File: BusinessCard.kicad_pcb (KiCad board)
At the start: 4 copper layers, 88.9 x 50.8 mm, 81 parts, among them J1 USB_OTG, J5 RNG, Q1 2N3904, Q2 2N3904, U1 TLE2426, U10 74HC74, U11 74HC74, U12 74HC74, U13 74HC74, U2 TLV271, U3 LM311, U4 74HC74, U5 INA826, U6 TLV272, U7 4066, U8 TLV272, U9 74HC14

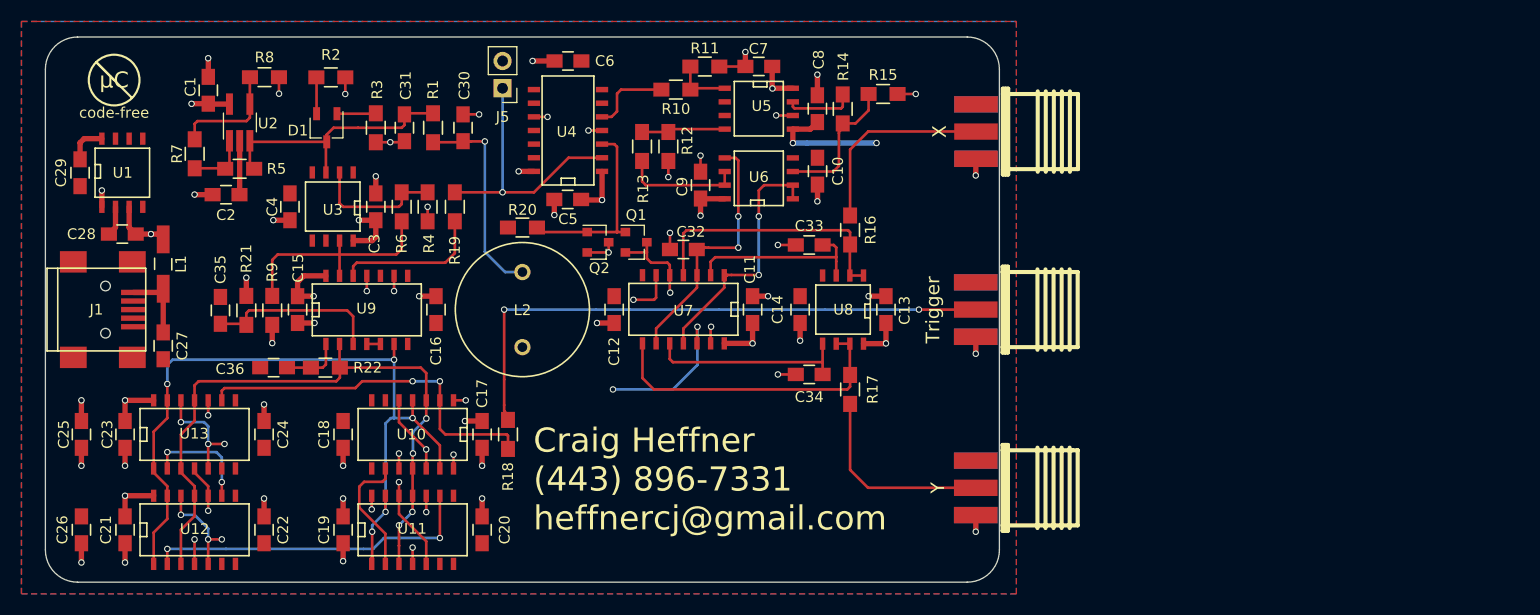
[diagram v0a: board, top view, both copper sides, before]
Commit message: All but the ring counter placed and routed.
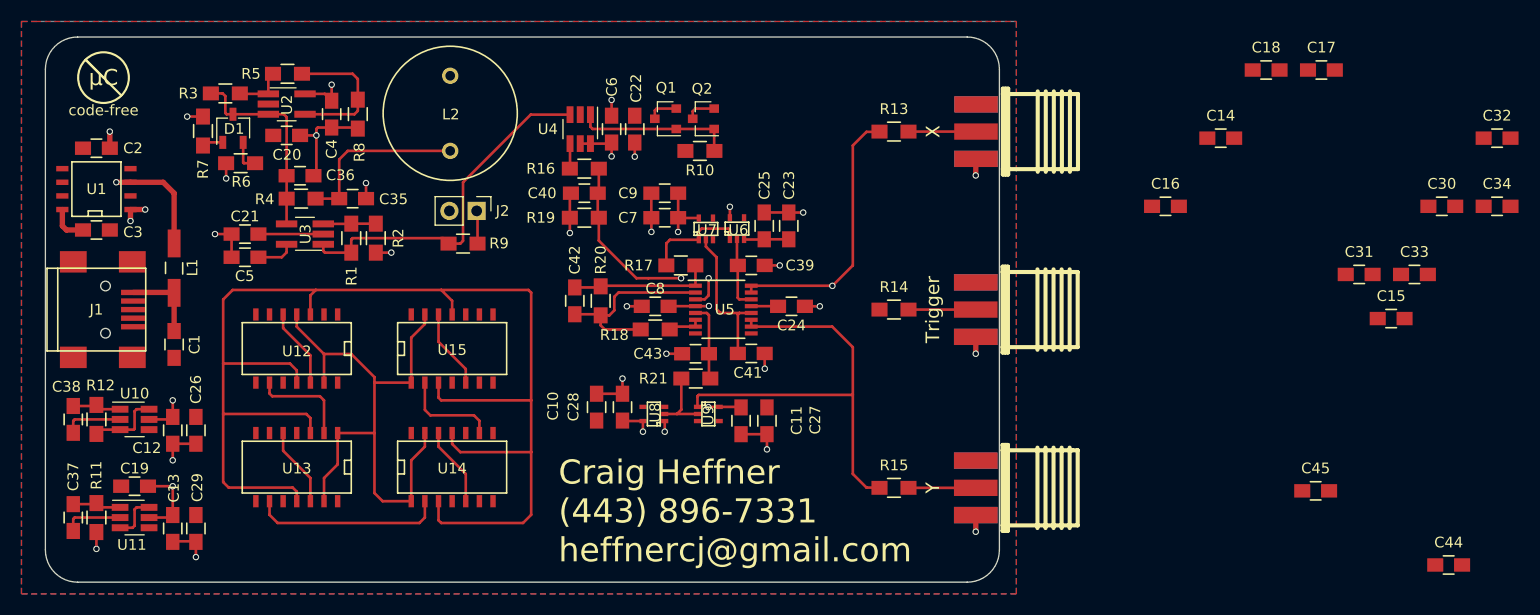
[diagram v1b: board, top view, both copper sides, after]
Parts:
- removed R22: 56k, Resistors_SMD:R_0805_HandSoldering
- removed Trigger: Trigger, CON-SMA-EDGE:CON-SMA-EDGE
- removed X: X, CON-SMA-EDGE:CON-SMA-EDGE
- removed Y: Y, CON-SMA-EDGE:CON-SMA-EDGE
- added C37: 0.1uF, Capacitors_SMD:C_0805_HandSoldering, F.Cu at (107.7, 116.1)
- added C38: 0.1uF, Capacitors_SMD:C_0805_HandSoldering, F.Cu at (107.7, 106.9)
- added C39: 1500pF, Capacitors_SMD:C_0805_HandSoldering, F.Cu at (170.9, 92.6)
- added C40: 1500pF, Capacitors_SMD:C_0805_HandSoldering, F.Cu at (155.3, 85.9)
- added C41: 1500pF, Capacitors_SMD:C_0805_HandSoldering, F.Cu at (170.9, 100.8)
- added C42: 1500pF, Capacitors_SMD:C_0805_HandSoldering, F.Cu at (154.4, 95.9)
- added C43: 1500pF, Capacitors_SMD:C_0805_HandSoldering, F.Cu at (165.7, 100.8)
- added C44: 10uF, Capacitors_SMD:C_0805_HandSoldering, F.Cu at (235.9, 120.5)
- added C45: 10uF, Capacitors_SMD:C_0805_HandSoldering, F.Cu at (223.5, 113.6)
- added J2: RNG, Pin_Headers:Pin_Header_Straight_1x02_Pitch2.54mm, F.Cu at (145.3, 87.5)
- added J3: X, CON-SMA-EDGE:CON-SMA-EDGE, F.Cu at (191.8, 80.1)
- added J4: Trigger, CON-SMA-EDGE:CON-SMA-EDGE, F.Cu at (191.8, 96.7)
- added U14: 74HC74, SMD_Packages:SOIC-14_N, F.Cu at (143.0, 111.3)
- added U15: 74HC74, SMD_Packages:SOIC-14_N, F.Cu at (143.0, 100.2)
- C18, C19, C2: value 0.1uF -> 10uF
- C25, C26, C28: value 10uF -> 0.1uF
- C31: value 0.01uF -> 0.1uF
- C32, C33: value 1500pF -> 0.1uF
- C34: value 1500pF -> 10uF
- C36: value 0.1uF -> 0.01uF
- J5: value RNG -> Y; footprint Pin_Headers:Pin_Header_Straight_1x02_Pitch2.54mm -> CON-SMA-EDGE:CON-SMA-EDGE
- R1: value 1.37k -> 1M
- R10: value 15k -> 2.2k
- R11: value 10k -> 10M
- R12: value 10k -> 56k
- R13, R14, R15: value 10k -> 2.2k
- R16, R18: value 2.2k -> 1.5k
- R17: value 2.2k -> 100
- R19, R20, R3: value 2.2k -> 1k
- R2: value 2.2k -> 100k
- R21: value 10M -> 100
- R4: value 100k -> 1.37k
- R6: value 1M -> 2.2k
- R7, R9: value 1k -> 2.2k
- U10, U11: value 74HC74 -> SN74LVC2G14DBVR; footprint SMD_Packages:SOIC-14_N -> TO_SOT_Packages_SMD:SOT-23-6_Handsoldering
- U3: value LM311 -> TLV3201; footprint SMD_Packages:SOIC-8-N -> TO_SOT_Packages_SMD:TSOT-23-5_HandSoldering
- U4: value 74HC74 -> SN74LVC1G175; footprint SMD_Packages:SOIC-14_N -> TO_SOT_Packages_SMD:SOT-23-6_Handsoldering
- U5: value INA826 -> LTC6242; footprint SMD_Packages:SOIC-8-N -> Housings_SSOP:SSOP-16_3.9x4.9mm_Pitch0.635mm
- U6, U8: value TLV272 -> SN74LVC1G66; footprint SMD_Packages:SOIC-8-N -> TO_SOT_Packages_SMD:SC-70-5
- U7: value 4066 -> SN74LVC1G66; footprint SMD_Packages:SOIC-14_N -> TO_SOT_Packages_SMD:SC-70-5
- U9: value 74HC14 -> SN74LVC1G66; footprint SMD_Packages:SOIC-14_N -> TO_SOT_Packages_SMD:SC-70-5
- moved C15 101.9 mm to (230.5, 97.5), turned to 0 degrees
- moved C18 92.5 mm to (218.9, 74.4), turned to 0 degrees
- moved C30 91.5 mm to (235.2, 87.1), turned to 0 degrees
- moved C31 90.0 mm to (227.5, 93.4), turned to 0 degrees
- moved C17 85.3 mm to (224.0, 74.4), turned to 0 degrees
- moved C32 76.5 mm to (240.4, 80.7), turned to 0 degrees
- moved R11 70.6 mm to (109.9, 116.1), turned to 90 degrees
- moved C13 69.5 mm to (117.0, 117.1), turned to 270 degrees
- moved C16 68.7 mm to (209.5, 87.1), turned to 0 degrees
- moved C25 66.5 mm to (172.1, 88.9)
- moved C34 66.0 mm to (240.4, 87.1), turned to 0 degrees
- moved C23 64.8 mm to (174.4, 88.9)
- moved R12 59.1 mm to (109.9, 106.9)
- moved J5 57.7 mm to (191.8, 113.3), turned to 90 degrees
- moved C27 56.7 mm to (172.3, 107.1), turned to 90 degrees
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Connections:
- C1 pad 1: +VDC -> Net-(C1-Pad1)
- C1 pad 2: GNDREF -> -VDC
- C10 pad 1: GNDREF -> +VDC
- C10 pad 2: -VDC -> GNDREF
- C12 pad 1: GNDREF -> +VDC
- C12 pad 2: -VDC -> GNDREF
- C14 pad 1: GNDREF -> +VDC
- C14 pad 2: -VDC -> GNDREF
- C16 pad 1: GNDREF -> +VDC
- C16 pad 2: -VDC -> GNDREF
- C18 pad 1: GNDREF -> +VDC
- C18 pad 2: -VDC -> GNDREF
- C19 pad 2: GNDREF -> -VDC
- C2 pad 1: GNDREF -> +VDC
- C21 pad 1: +VDC -> GNDREF
- C21 pad 2: GNDREF -> -VDC
- C23 pad 1: +VDC -> GNDREF
- C23 pad 2: GNDREF -> -VDC
- C25 pad 1: +VDC -> GNDREF
- C25 pad 2: GNDREF -> -VDC
- C27 pad 1: Net-(C27-Pad1) -> GNDREF
- C28 pad 1: +VDC -> GNDREF
- C29 pad 1: Net-(C29-Pad1) -> GNDREF
- C3 pad 1: +VDC -> Net-(C3-Pad1)
- C3 pad 2: GNDREF -> -VDC
- C30 pad 1: Net-(C30-Pad1) -> GNDREF
- C30 pad 2: GNDREF -> -VDC
- C31 pad 1: Net-(C31-Pad1) -> GNDREF
- C31 pad 2: GNDREF -> -VDC
- C32 pad 1: Net-(C32-Pad1) -> GNDREF
- C32 pad 2: GNDREF -> -VDC
- C33 pad 1: Net-(C33-Pad1) -> GNDREF
- C33 pad 2: GNDREF -> -VDC
- C34 pad 1: Net-(C34-Pad1) -> GNDREF
- C34 pad 2: GNDREF -> -VDC
- C35 pad 2: -VDC -> GNDREF
- C36 pad 2: -VDC -> GNDREF
- C4 pad 1: GNDREF -> +VDC
- C4 pad 2: -VDC -> GNDREF
- C6 pad 1: GNDREF -> +VDC
- C6 pad 2: -VDC -> GNDREF
- C8 pad 1: GNDREF -> +VDC
- C8 pad 2: -VDC -> GNDREF
- D1 pad 3: Net-(C31-Pad1) -> Net-(C36-Pad1)
- J1 pad 1: Net-(C27-Pad1) -> Net-(C1-Pad1)
- J5 pad 2: -VDC -> GNDREF
- L1 pad 1: Net-(C27-Pad1) -> Net-(C1-Pad1)
- L2 pad 2: Net-(C30-Pad1) -> Net-(C35-Pad1)
- R1 pad 1: Net-(C30-Pad1) -> CHUA_ATTRACTOR
- R1 pad 2: Net-(C31-Pad1) -> Net-(R1-Pad2)
- R10 pad 1: COORDINATE -> Net-(Q1-Pad1)
- R10 pad 2: Net-(R10-Pad2) -> -VDC
- R11 pad 1: Net-(R10-Pad2) -> +VDC
- R11 pad 2: GNDREF -> Net-(C37-Pad1)
- R12 pad 1: Net-(R12-Pad1) -> Net-(C38-Pad1)
- R12 pad 2: GNDREF -> Net-(R12-Pad2)
- R13 pad 1: Net-(R12-Pad1) -> FRACTAL_X
- R13 pad 2: Net-(R13-Pad2) -> Net-(J3-Pad1)
- R14 pad 1: Net-(R14-Pad1) -> FRACTAL_TRIGGER
- R14 pad 2: Net-(R14-Pad2) -> Net-(J4-Pad1)
- R15 pad 1: Net-(R14-Pad2) -> FRACTAL_Y
- R15 pad 2: GNDREF -> Net-(J5-Pad1)
- R16 pad 1: FRACTAL_X -> COORDINATE
- R16 pad 2: Net-(J2-Pad1) -> Net-(C40-Pad1)
- R17 pad 1: FRACTAL_Y -> Net-(R17-Pad1)
- R17 pad 2: Net-(J3-Pad1) -> Net-(C42-Pad1)
- R18 pad 1: FRACTAL_TRIGGER -> Net-(R18-Pad1)
- R18 pad 2: Net-(J4-Pad1) -> Net-(C42-Pad2)
- R19 pad 1: CHUA_ATTRACTOR -> Net-(C40-Pad1)
- R19 pad 2: Net-(J5-Pad1) -> GNDREF
- R2 pad 1: Net-(D1-Pad2) -> Net-(R1-Pad2)
- R20 pad 1: Net-(Q1-Pad1) -> Net-(C42-Pad1)
- R20 pad 2: -VDC -> Net-(C42-Pad2)
- R21 pad 1: +VDC -> Net-(R21-Pad1)
- R21 pad 2: Net-(C35-Pad1) -> Net-(C43-Pad1)
- R3 pad 1: Net-(D1-Pad1) -> Net-(C36-Pad1)
- R3 pad 2: GNDREF -> Net-(R3-Pad2)
- R4 pad 1: Net-(R4-Pad1) -> Net-(C35-Pad1)
- R4 pad 2: GNDREF -> Net-(C36-Pad1)
- R5 pad 1: Net-(C31-Pad1) -> Net-(R3-Pad2)
- R6 pad 1: Net-(R6-Pad1) -> Net-(D1-Pad2)
- R6 pad 2: Net-(R4-Pad1) -> GNDREF
- R7 pad 1: Net-(R5-Pad2) -> Net-(D1-Pad1)
- R7 pad 2: Net-(R7-Pad2) -> GNDREF
- R8 pad 1: Net-(R7-Pad2) -> Net-(R5-Pad2)
- R9 pad 1: +VDC -> CHUA_ATTRACTOR
- R9 pad 2: Net-(R6-Pad1) -> Net-(J2-Pad1)
- U1 pad 8: Net-(C29-Pad1) -> Net-(C3-Pad1)
- U10 pad 1: +VDC -> Net-(C38-Pad1)
- U10 pad 2: FRACTAL_TRIGGER -> -VDC
- U10 pad 3: CLOCK -> Net-(R12-Pad2)
- U10 pad 4: RESET -> CLOCK
- U10 pad 5: CLOCK_CYCLE_0 -> +VDC
- U10 pad 6: Net-(U10-Pad6) -> Net-(R12-Pad2)
- U11 pad 1: RESET -> Net-(C37-Pad1)
- U11 pad 2: Net-(U10-Pad9) -> -VDC
- U11 pad 3: CLOCK -> Net-(U11-Pad3)
- U11 pad 4: +VDC -> RESET
- U11 pad 5: CLOCK_CYCLE_1 -> +VDC
- U11 pad 6: Net-(U11-Pad6) -> Net-(U11-Pad3)
- U12 pad 1: RESET -> +VDC
- U12 pad 12: CLOCK_CYCLE_2 -> CLOCK_CYCLE_0
- U12 pad 2: Net-(U11-Pad9) -> FRACTAL_TRIGGER
- U12 pad 4: +VDC -> RESET
- U12 pad 5: CLOCK_CYCLE_2 -> CLOCK_CYCLE_0
- U13 pad 12: CLOCK_CYCLE_3 -> CLOCK_CYCLE_1
- U13 pad 5: CLOCK_CYCLE_3 -> CLOCK_CYCLE_1
- U13 pad 9: FRACTAL_TRIGGER -> Net-(U13-Pad9)
- U2 pad 1: Net-(R5-Pad2) -> Net-(R3-Pad2)
- U2 pad 3: Net-(C31-Pad1) -> Net-(C36-Pad1)
- U2 pad 4: Net-(R7-Pad2) -> Net-(R5-Pad2)
- U3 pad 1: -VDC -> CHUA_ATTRACTOR
- U3 pad 2: Net-(R4-Pad1) -> -VDC
- U3 pad 3: Net-(C31-Pad1) -> Net-(R1-Pad2)
- U3 pad 4: -VDC -> Net-(C36-Pad1)
- U3 pad 5: Net-(U3-Pad5) -> +VDC
- U4 pad 1: +VDC -> Net-(Q1-Pad1)
- U4 pad 2: Net-(J5-Pad1) -> -VDC
- U4 pad 3: Net-(Q1-Pad1) -> CHUA_ATTRACTOR
- U4 pad 4: +VDC -> COORDINATE
- U4 pad 5: COORDINATE -> +VDC
- U4 pad 6: Net-(U4-Pad6) -> +VDC
- U5 pad 1: Net-(R10-Pad2) -> Net-(C42-Pad1)
- U5 pad 2: Net-(U5-Pad2) -> Net-(C42-Pad2)
- U5 pad 3: Net-(U5-Pad3) -> Net-(C40-Pad1)
- U5 pad 4: Net-(R12-Pad1) -> +VDC
- U5 pad 5: -VDC -> Net-(C43-Pad1)
- U5 pad 6: GNDREF -> Net-(R18-Pad1)
- U5 pad 7: Net-(R14-Pad1) -> Net-(R18-Pad1)
- U5 pad 8: +VDC -> Net-(U5-Pad8)
- U6 pad 1: Net-(U6-Pad1) -> Net-(R17-Pad1)
- U6 pad 2: Net-(U6-Pad1) -> Net-(C39-Pad1)
- U6 pad 3: Net-(R14-Pad2) -> -VDC
- U6 pad 4: -VDC -> CLOCK_CYCLE_1
- U6 pad 5: Net-(C32-Pad1) -> +VDC
- U7 pad 1: Net-(U6-Pad1) -> Net-(R17-Pad1)
- U7 pad 2: Net-(C33-Pad1) -> Net-(C41-Pad1)
- U7 pad 3: Net-(C32-Pad1) -> -VDC
- U7 pad 4: FRACTAL_X -> CLOCK_CYCLE_3
- U7 pad 5: CLOCK_CYCLE_0 -> +VDC
- U8 pad 2: FRACTAL_X -> Net-(R21-Pad1)
- U8 pad 3: Net-(C33-Pad1) -> -VDC
- U8 pad 4: -VDC -> CLOCK_CYCLE_0
- U8 pad 5: Net-(C34-Pad1) -> +VDC
- U9 pad 1: Net-(C36-Pad1) -> FRACTAL_Y
- U9 pad 2: CLOCK -> Net-(R21-Pad1)
- U9 pad 3: Net-(C35-Pad1) -> -VDC
- U9 pad 4: Net-(U9-Pad4) -> CLOCK_CYCLE_2
- U9 pad 5: Net-(U9-Pad4) -> +VDC
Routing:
- net CLOCK_CYCLE_2: track 87.4 -> 10.2 mm, vias 5 -> 0
- net CLOCK: track 62.3 -> 127.8 mm, vias 4 -> 0
- net CLOCK_CYCLE_3: track 63.8 -> 7.40 mm, vias 5 -> 0
- net Net-(J4-Pad1): track 54.4 -> 6.27 mm, vias 2 -> 0
- net CLOCK_CYCLE_1: track 52.2 -> 7.40 mm, vias 2 -> 0
- net CLOCK_CYCLE_0: track 52.0 -> 10.3 mm, vias 2 -> 0
- net FRACTAL_TRIGGER: track 33.9 -> 0.00 mm, vias 2 -> 0
- net Net-(U11-Pad9): track 31.2 -> 0.00 mm, vias 2 -> 0
- net +VDC: track 82.3 -> 53.1 mm, vias 30 -> 12
- net FRACTAL_X: track 25.0 -> 52.6 mm, vias 0 -> 2
- net Net-(C31-Pad1): track 25.7 -> 0.00 mm
- net Net-(C32-Pad1): track 23.8 -> 0.00 mm, vias 2 -> 0
- net Net-(U6-Pad1): track 23.7 -> 0.00 mm, vias 2 -> 0
- net Net-(R6-Pad1): track 21.7 -> 0.00 mm
- net Net-(C40-Pad1): track 0.00 -> 21.6 mm, vias 0 -> 2
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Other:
- board text added: "0.506127"
- board text added: "Horizontal: XY mode CH1, CH2: 500mV/div Aquisition: High resolution Display: Infinite persistence Trigger: Rising edge, +-2.5V http://www.analogzoo.com/businesscard"
- board text removed: "http://www.analogzoo.com/businesscard"

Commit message: All parts placed, only routing of clock signals remain.
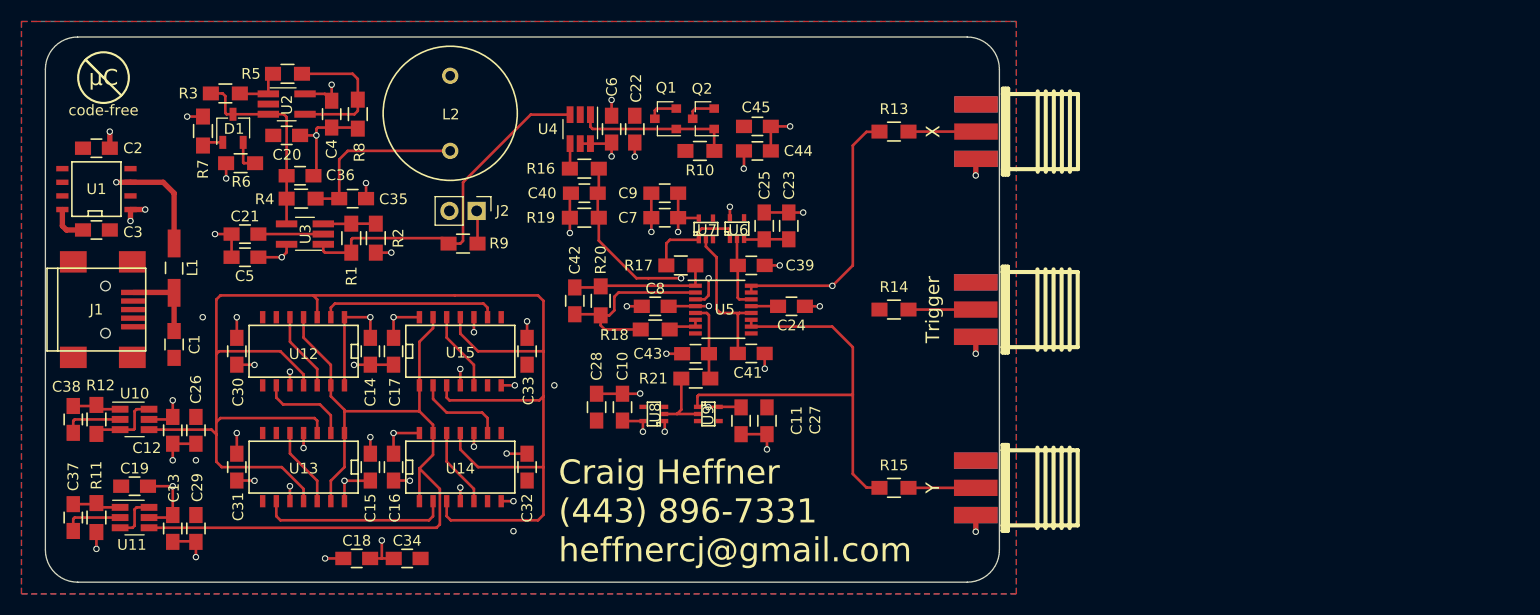
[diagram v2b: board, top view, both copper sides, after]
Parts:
- moved C30 113.1 mm to (122.9, 100.6), turned to 90 degrees
- moved C34 106.7 mm to (138.8, 119.9)
- moved C31 106.1 mm to (122.9, 111.4), turned to 90 degrees
- moved C18 96.2 mm to (134.1, 119.9)
- moved C15 96.1 mm to (135.4, 111.4), turned to 90 degrees
- moved C32 95.4 mm to (150.0, 111.4), turned to 270 degrees
- moved C17 90.3 mm to (137.5, 100.6), turned to 270 degrees
- moved C33 83.0 mm to (150.0, 100.6), turned to 270 degrees
- moved C14 81.7 mm to (135.4, 100.6), turned to 270 degrees
- moved C16 75.9 mm to (137.5, 111.4), turned to 270 degrees
- moved C44 75.1 mm to (171.4, 81.9)
- moved C45 62.1 mm to (171.4, 79.6), turned to 180 degrees
- moved U15 0.80 mm to (143.8, 100.5)
- moved U14 0.76 mm to (143.8, 111.3)
- moved U12 0.68 mm to (129.2, 100.7)
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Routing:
- net +VDC: track 53.1 -> 89.7 mm, vias 12 -> 26
- net RESET: track 55.0 -> 78.2 mm
- net GNDREF: track 62.6 -> 84.3 mm, vias 25 -> 34
- net -VDC: track 23.8 -> 44.8 mm, vias 0 -> 8
- net CLOCK: track 127.8 -> 146.9 mm
- net FRACTAL_TRIGGER: track 0.00 -> 16.7 mm
- net Net-(U12-Pad9): track 9.41 -> 8.56 mm
- net Net-(U14-Pad9): track 9.18 -> 8.48 mm

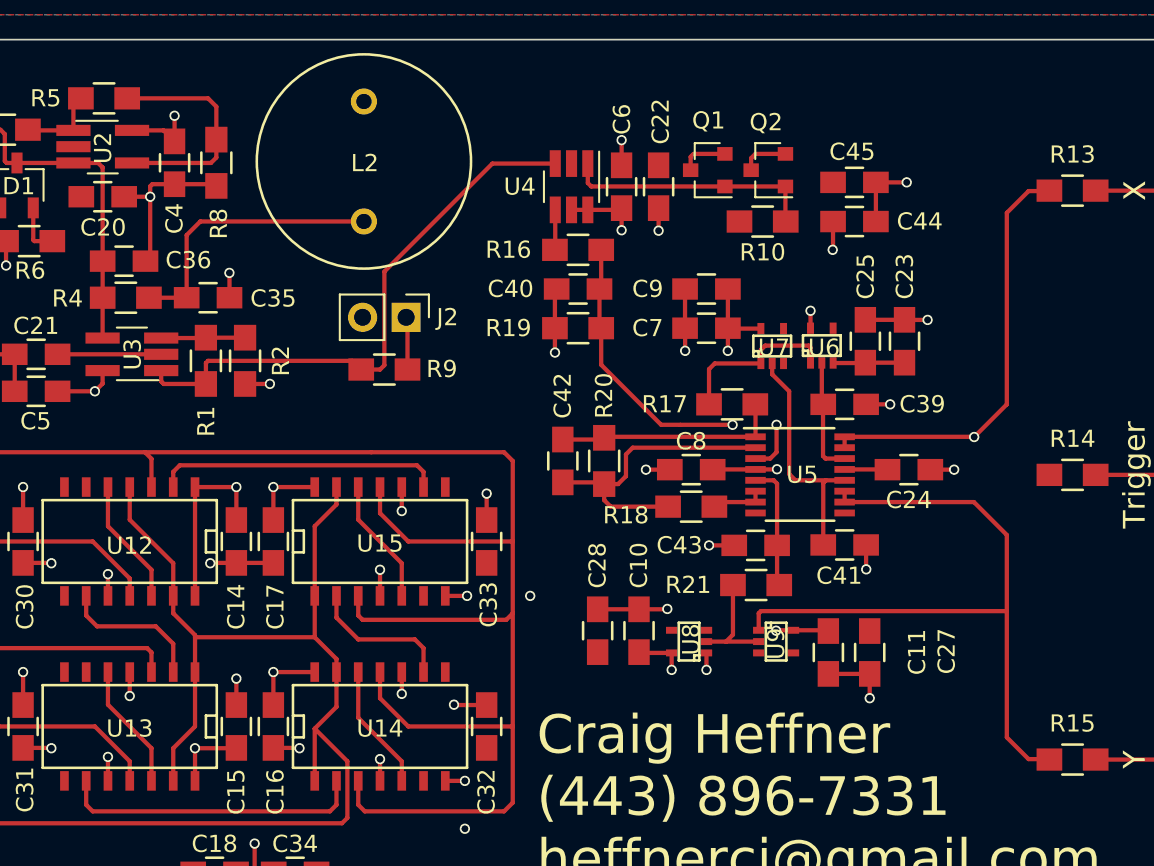
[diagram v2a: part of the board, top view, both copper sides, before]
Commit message: Final PCB routing, generated Gerber files.
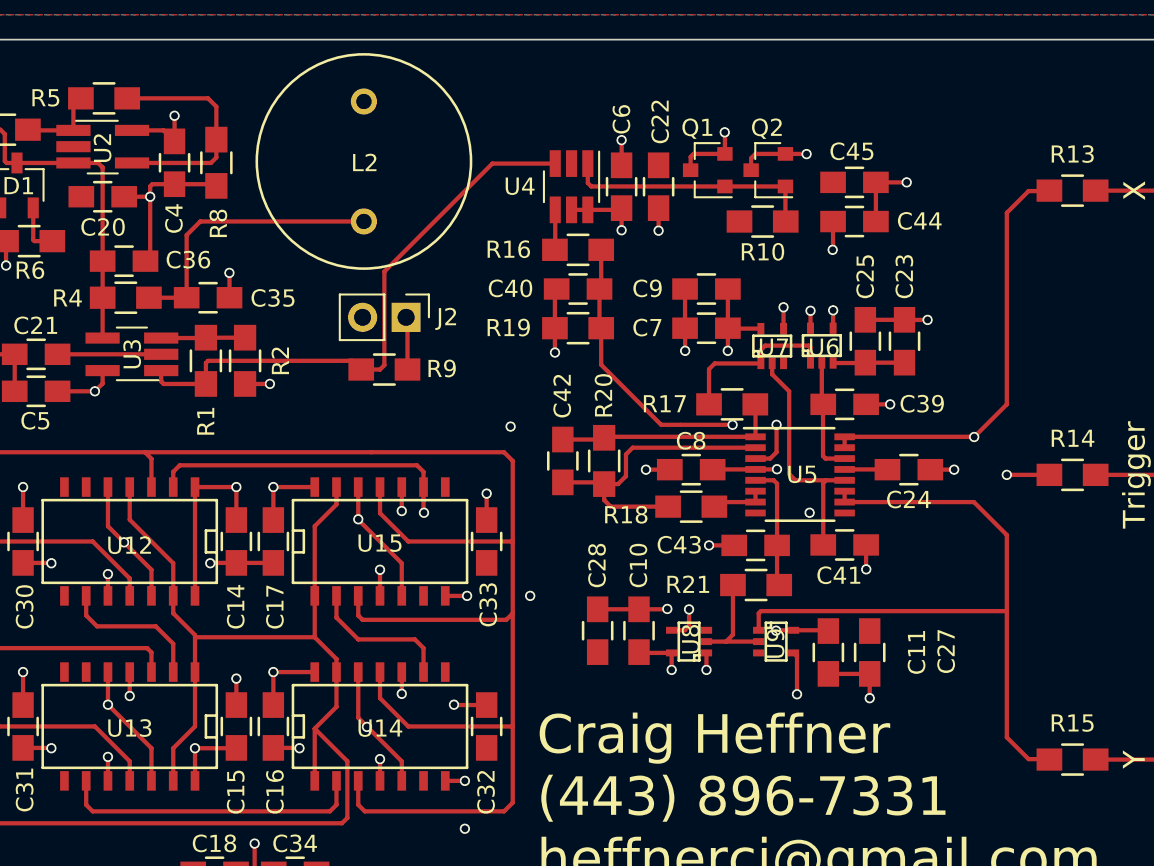
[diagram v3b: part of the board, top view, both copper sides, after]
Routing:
- net CLOCK_CYCLE_0: track 10.3 -> 75.8 mm, vias 0 -> 3
- net CLOCK_CYCLE_1: track 7.40 -> 72.0 mm, vias 0 -> 3
- net CLOCK_CYCLE_2: track 10.2 -> 71.7 mm, vias 0 -> 3
- net FRACTAL_TRIGGER: track 16.7 -> 55.6 mm, vias 0 -> 3
- net CLOCK_CYCLE_3: track 7.40 -> 38.6 mm, vias 0 -> 2
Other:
- net class Default: clearance 0.25 -> 0.2
- rule trace_clearance: 0.25 -> 0.2
